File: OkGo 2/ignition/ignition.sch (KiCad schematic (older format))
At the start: 45 parts, among them K101 16A SPST, P102 JST_XH_4WAY, P103 BATT, P104 BATT, P105 PPOLE, P106 PPOLE, P107 CHARGE_CASE, P108 SMA, SW101 LATCHING PUSH, U101 SWD, U102 FUSE 15A, U103 CLIP, U104 BEZEL, U105 RFM95W, U106 STM32F071CBT6, U107 TSR 0.5-2433, Y101 8MHz

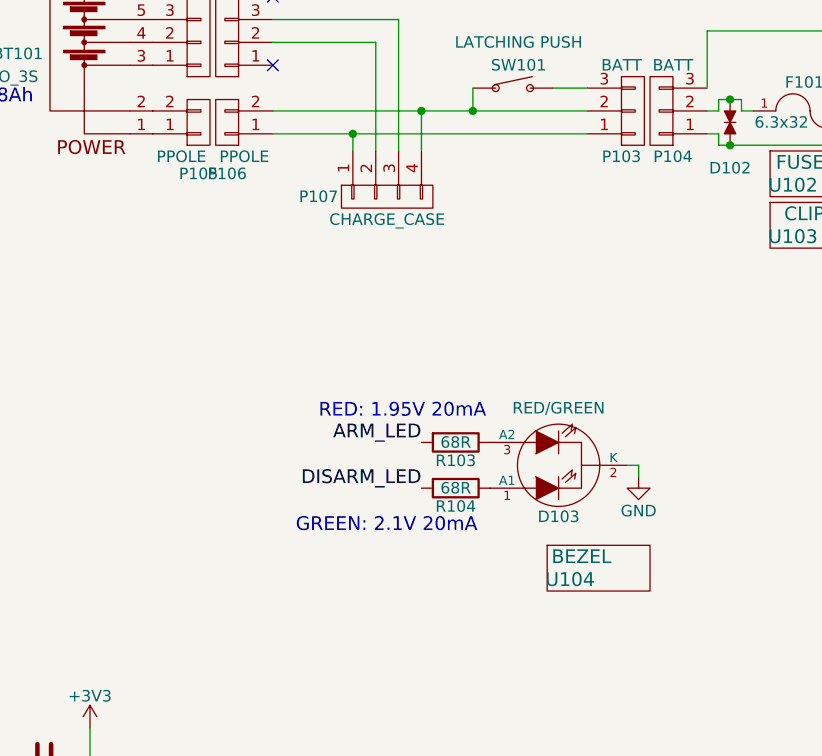
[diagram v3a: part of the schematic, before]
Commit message: 4-bit LCD, pulldowns, 2-pin bicolour ARM LED
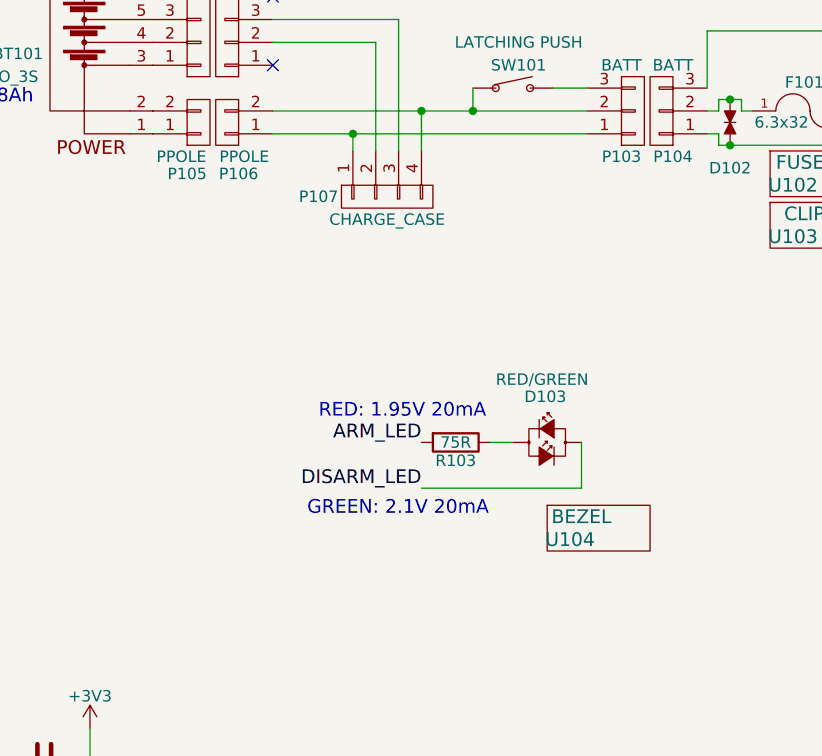
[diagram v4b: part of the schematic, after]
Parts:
- removed D103: RED/GREEN, symbol Led_x2
- removed R104: 68R, Resistors_SMD:R_0805, symbol R
- added D103: RED/GREEN, symbol LED_bicolour
- R103: value 68R -> 75R; Farnell 2332055 -> 2331781
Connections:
- net DISARM_LED: now also D103.2 (A)
- net at R103.1: now also D103.1 (K)
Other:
- moved on the sheet: U104
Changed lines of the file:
@@
 LIBS:push_illum
 LIBS:push_illum_straight
+LIBS:led_bicolour
 LIBS:ignition-cache
 EELAYER 25 0
@@
 $EndComp
 $Comp
-L Led_x2 D103
-U 1 1 55A8E3E4
-P 3500 2800
-F 0 "D103" H 3500 3025 50  0000 C CNN
-F 1 "RED/GREEN" H 3500 2550 50  0000 C CNN
-F 2 "" H 3500 2800 60  0000 C CNN
-F 3 "" H 3500 2800 60  0000 C CNN
-F 4 "2449761" H 3500 2800 60  0001 C CNN "Farnell"
-	1    3500 2800
-	-1   0    0    1
-$EndComp
-$Comp
-L GND #PWR021
-U 1 1 55A8E7EB
-P 3850 2850
-F 0 "#PWR021" H 3850 2600 50  0001 C CNN
-F 1 "GND" H 3850 2700 50  0000 C CNN
-F 2 "" H 3850 2850 60  0000 C CNN
-F 3 "" H 3850 2850 60  0000 C CNN
-	1    3850 2850
-	1    0    0    -1
-$EndComp
-$Comp
 L R R103
 U 1 1 55A8E9D5
 P 3050 2700
 F 0 "R103" V 3130 2700 50  0000 C CNN
-F 1 "68R" V 3050 2700 50  0000 C CNN
+F 1 "75R" V 3050 2700 50  0000 C CNN
 F 2 "Resistors_SMD:R_0805" V 2980 2700 30  0001 C CNN
 F 3 "" H 3050 2700 30  0000 C CNN
-F 4 "2332055" H 3050 2700 60  0001 C CNN "Farnell"
+F 4 "2331781" H 3050 2700 60  0001 C CNN "Farnell"
 	1    3050 2700
-	0    1    1    0
-$EndComp
-$Comp
-L R R104
-U 1 1 55A8EA84
-P 3050 2900
-F 0 "R104" V 3130 2900 50  0000 C CNN
-F 1 "68R" V 3050 2900 50  0000 C CNN
-F 2 "Resistors_SMD:R_0805" V 2980 2900 30  0001 C CNN
-F 3 "" H 3050 2900 30  0000 C CNN
-F 4 "2332055" H 3050 2900 60  0001 C CNN "Farnell"
-	1    3050 2900
 	0    1    1    0
 $EndComp
@@
 L PART U104
 U 1 1 55A94007
-P 3500 3300
-F 0 "U104" H 3550 3300 60  0000 C CNN
-F 1 "BEZEL" H 3600 3400 60  0000 C CNN
-F 2 "" H 3500 3300 60  0000 C CNN
-F 3 "" H 3500 3300 60  0000 C CNN
-F 4 "SC11628" H 3500 3300 60  0001 C CNN "Farnell"
-	1    3500 3300
+P 3500 3125
+F 0 "U104" H 3550 3125 60  0000 C CNN
+F 1 "BEZEL" H 3600 3225 60  0000 C CNN
+F 2 "" H 3500 3125 60  0000 C CNN
+F 3 "" H 3500 3125 60  0000 C CNN
+F 4 "SC11628" H 3500 3125 60  0001 C CNN "Farnell"
+	1    3500 3125
 	1    0    0    -1
 $EndComp
 Text Notes 2450 2600 0    60   ~ 0
 RED: 1.95V 20mA
-Text Notes 2350 3100 0    60   ~ 0
+Text Notes 2400 3025 0    60   ~ 0
 GREEN: 2.1V 20mA
 $Comp
@@
 Wire Wire Line
 	3475 1150 3625 1150
-Wire Wire Line
-	3850 2850 3850 2800
-Wire Wire Line
-	3850 2800 3800 2800
 Wire Wire Line
 	6650 6400 6650 6250
@@
 U 1 1 55AB8DCF
 P 2050 1300
-F 0 "P106" H 2050 1525 50  0000 C CNN
+F 0 "P106" H 2000 1525 50  0000 C CNN
 F 1 "PPOLE" H 1975 1450 50  0000 C CNN
 F 2 "" H 2050 1300 60  0000 C CNN
@@
 U 1 1 55ABB267
 P 1925 1300
-F 0 "P105" H 1925 1525 50  0000 C CNN
+F 0 "P105" H 1875 1525 50  0000 C CNN
 F 1 "PPOLE" H 1850 1450 50  0000 C CNN
 F 2 "" H 1925 1300 60  0000 C CNN
@@
 	2900 1250 2900 1425
 Connection ~ 2900 1250
+$Comp
+L LED_bicolour D103
+U 1 1 55BB39DE
+P 3450 2700
+F 0 "D103" H 3350 2900 50  0000 L CNN
+F 1 "RED/GREEN" H 3225 2975 50  0000 L CNN
+F 2 "" V 3450 2760 60  0000 C CNN
+F 3 "" V 3450 2760 60  0000 C CNN
+F 4 "1581207" H 3450 2700 60  0001 C CNN "Farnell"
+	1    3450 2700
+	1    0    0    -1
+$EndComp
+Wire Wire Line
+	2900 2900 3600 2900
+Wire Wire Line
+	3200 2700 3300 2700
+Wire Wire Line
+	3600 2900 3600 2700
 $EndSCHEMATC

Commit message: Finished demo-route of control
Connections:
- net GND: now also U106.44 (BOOT0)
- net nRST: now also U106.7 (NRST); no longer U106.44 (BOOT0)
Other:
- moved on the sheet: C104, TP103
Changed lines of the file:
@@
 L C C104
 U 1 1 5562F811
-P 4000 4600
-F 0 "C104" H 3900 4700 50  0000 L CNN
-F 1 "100n" H 3800 4500 50  0000 L CNN
-F 2 "Capacitors_SMD:C_0805" H 4038 4450 30  0001 C CNN
-F 3 "" H 4000 4600 60  0000 C CNN
-F 4 "2407344" H 4000 4600 60  0001 C CNN "Farnell"
-	1    4000 4600
+P 4000 4500
+F 0 "C104" H 3900 4600 50  0000 L CNN
+F 1 "100n" H 3800 4400 50  0000 L CNN
+F 2 "Capacitors_SMD:C_0805" H 4038 4350 30  0001 C CNN
+F 3 "" H 4000 4500 60  0000 C CNN
+F 4 "2407344" H 4000 4500 60  0001 C CNN "Farnell"
+	1    4000 4500
 	-1   0    0    -1
 $EndComp
@@
 L GND #PWR013
 U 1 1 5562F9AC
-P 3950 4800
-F 0 "#PWR013" H 3950 4550 50  0001 C CNN
-F 1 "GND" H 3950 4650 50  0000 C CNN
-F 2 "" H 3950 4800 60  0000 C CNN
-F 3 "" H 3950 4800 60  0000 C CNN
-	1    3950 4800
+P 3950 4700
+F 0 "#PWR013" H 3950 4450 50  0001 C CNN
+F 1 "GND" H 3950 4550 50  0000 C CNN
+F 2 "" H 3950 4700 60  0000 C CNN
+F 3 "" H 3950 4700 60  0000 C CNN
+	1    3950 4700
 	-1   0    0    -1
 $EndComp
@@
 Text Label 5900 5550 0    60   ~ 0
 RFM_RESET
-Text Label 4200 4450 0    60   ~ 0
+Text Label 4200 4350 0    60   ~ 0
 nRST
 $Comp
@@
 L TestPoint TP103
 U 1 1 559DC7C1
-P 3850 4450
-F 0 "TP103" H 3850 4375 60  0000 C CNN
-F 1 "nRST" H 3825 4275 60  0000 C CNN
-F 2 "common:TESTPOINT" H 3850 4450 60  0001 C CNN
-F 3 "" H 3850 4450 60  0000 C CNN
-	1    3850 4450
+P 3850 4350
+F 0 "TP103" H 3850 4275 60  0000 C CNN
+F 1 "nRST" H 3825 4175 60  0000 C CNN
+F 2 "common:TESTPOINT" H 3850 4350 60  0001 C CNN
+F 3 "" H 3850 4350 60  0000 C CNN
+	1    3850 4350
 	-1   0    0    1
 $EndComp
@@
 Connection ~ 1800 5450
 Wire Wire Line
-	3850 4750 4000 4750
-Wire Wire Line
-	3950 4750 3950 4800
-Connection ~ 3950 4750
-Wire Wire Line
-	3750 4450 4200 4450
-Wire Wire Line
-	3750 4450 3750 4700
-Wire Wire Line
-	3750 4700 3300 4700
-Wire Wire Line
-	3850 4750 3850 4800
-Wire Wire Line
-	3850 4800 3300 4800
+	3850 4650 4000 4650
+Wire Wire Line
+	3950 4650 3950 4700
+Connection ~ 3950 4650
+Wire Wire Line
+	3750 4350 4200 4350
+Wire Wire Line
+	3750 4350 3750 4600
+Wire Wire Line
+	3750 4600 3300 4600
+Wire Wire Line
+	3850 4650 3850 4700
+Wire Wire Line
+	3850 4700 3300 4700
 Wire Wire Line
 	3300 5300 4100 5300
@@
 Wire Wire Line
 	8800 6050 8750 6050
-Connection ~ 4000 4450
+Connection ~ 4000 4350
 Connection ~ 6350 1150
 Connection ~ 6350 1250
 Connection ~ 6550 6400
-Connection ~ 3850 4450
+Connection ~ 3850 4350
 Wire Wire Line
 	3300 5400 3750 5400

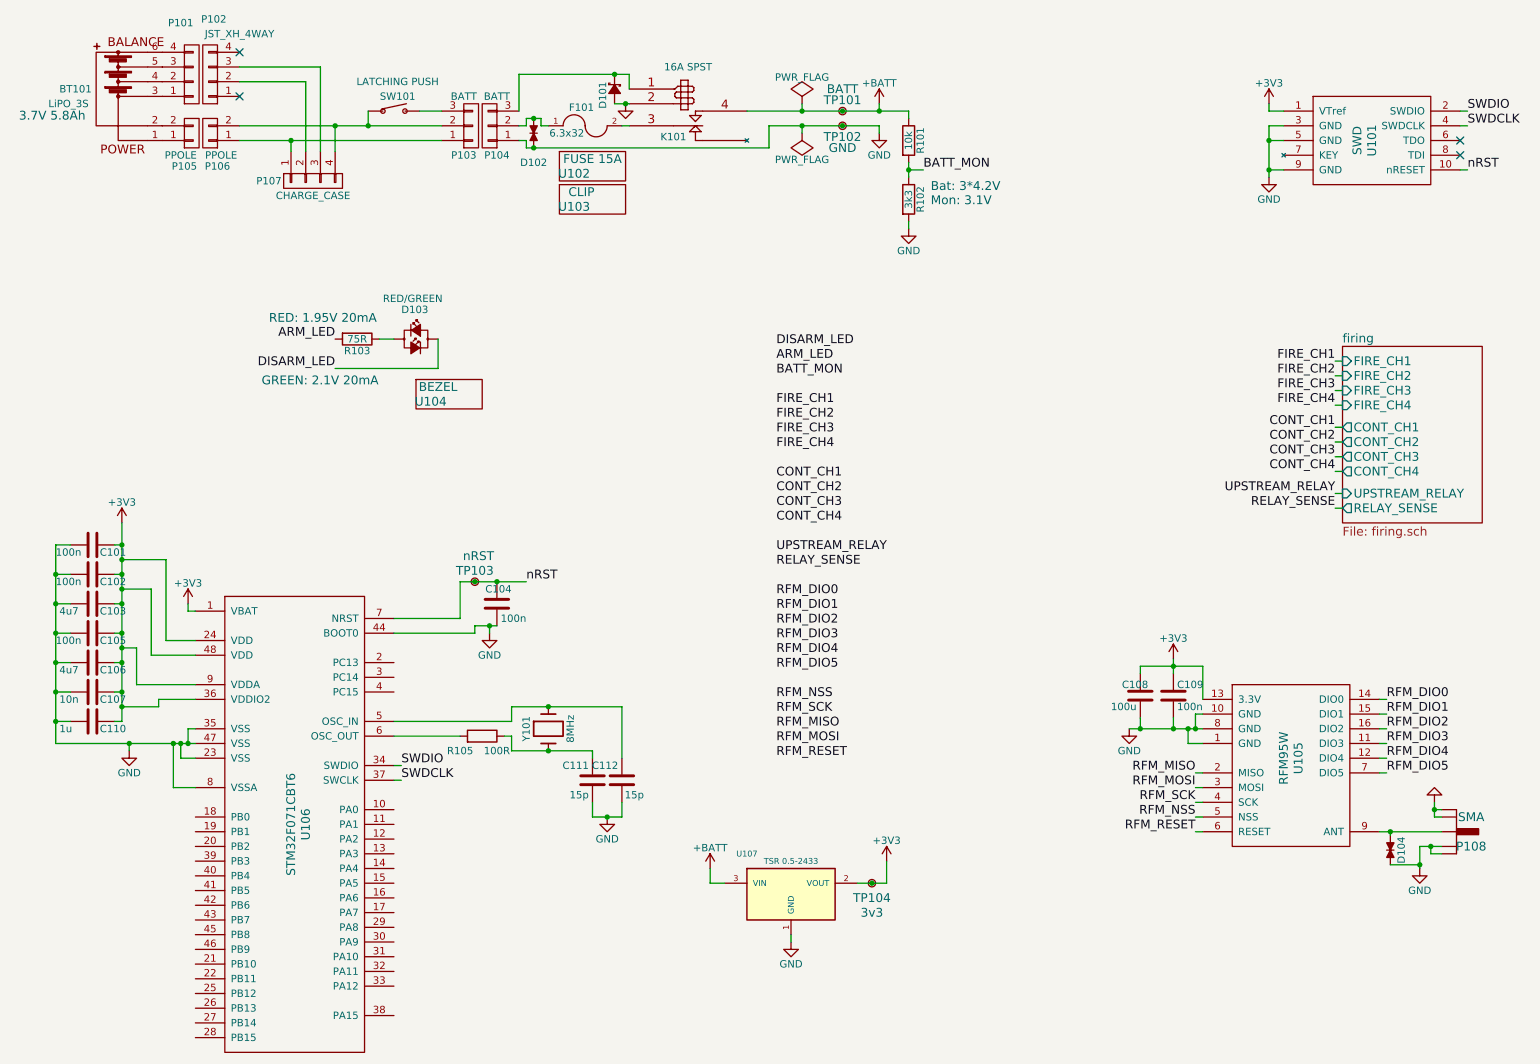
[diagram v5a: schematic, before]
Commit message: Footprinting, rockers
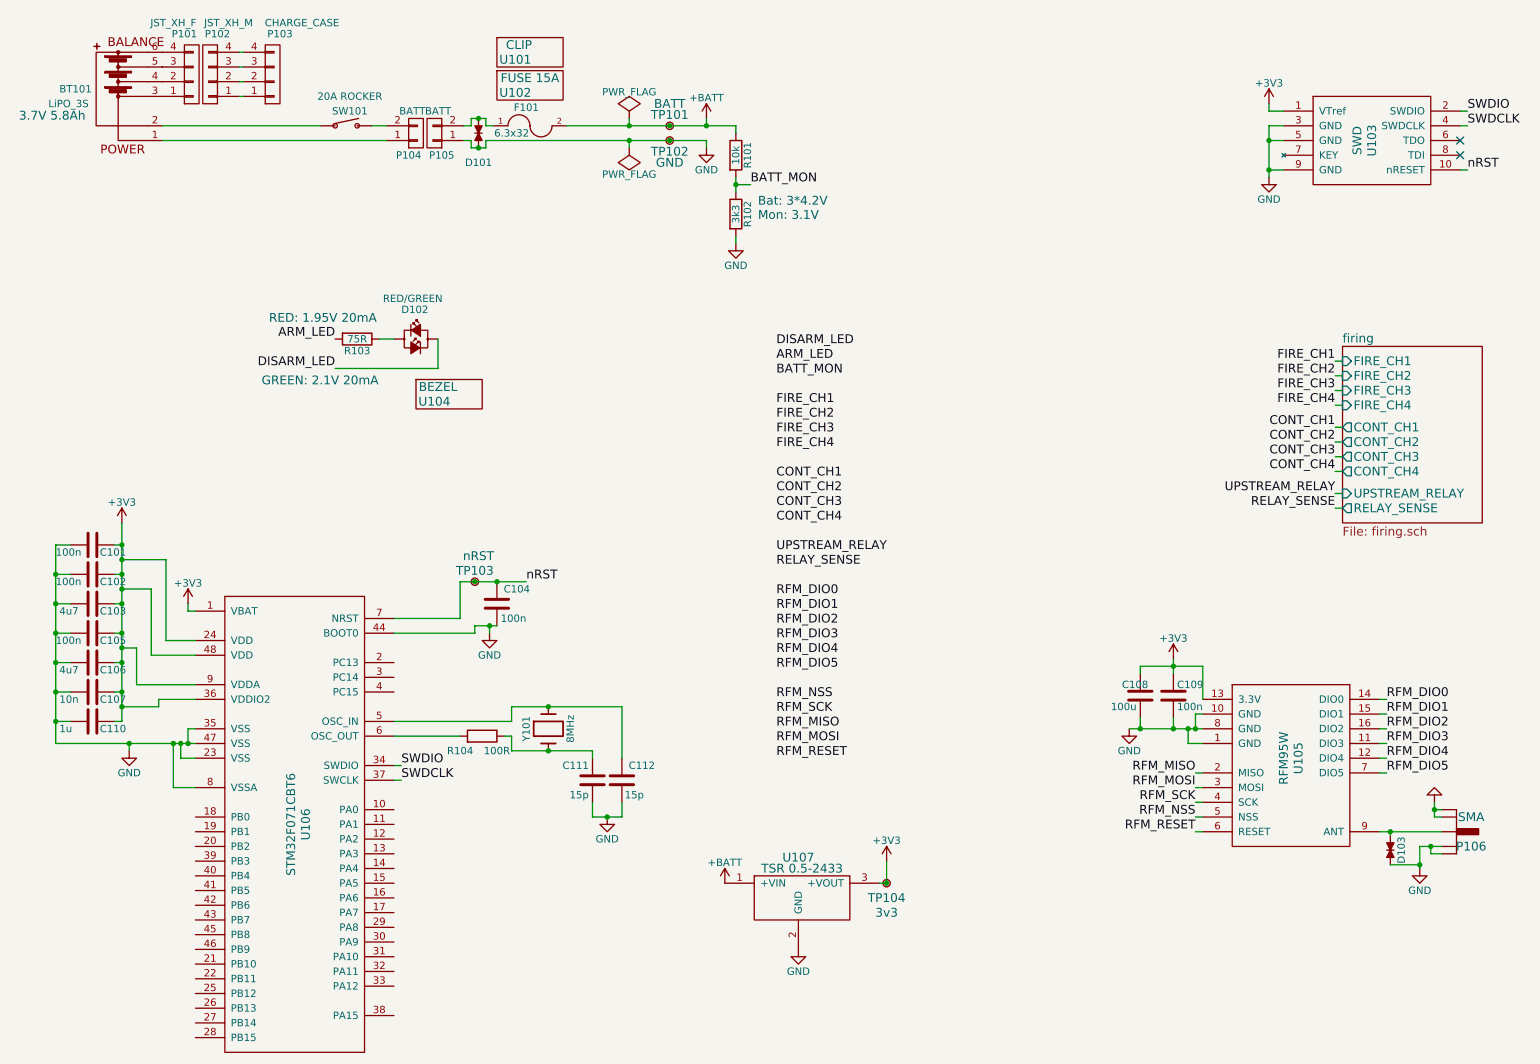
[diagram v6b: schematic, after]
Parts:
- removed D101: MBR2H200SFT1G, ignition:SOD-123FL, symbol D_Schottky_Small
- removed K101: 16A SPST, ignition:Relay_RT314, symbol RELAY_SPST
- removed P103, P104: BATT, symbol CONN_01X03
- removed P106: PPOLE, symbol CONN_01X02
- removed U107: TSR 0.5-2433, SOT-23, symbol APE8865N-33-HF-3
- added P104: BATT, symbol CONN_01X02
- added U107: TSR 0.5-2433, ignition:TSR-0_5, symbol TSR-0_5
- P101: value ~ -> JST_XH_F
- P102: value JST_XH_4WAY -> JST_XH_M
- P105: value PPOLE -> BATT; footprint (none) -> ignition:PCB_SPADE; Farnell (none) -> 2308798
- SW101: value LATCHING PUSH -> 20A ROCKER; Farnell SW02719 -> 1839503
- renumbered D102 to D101, D103 to D102, D104 to D103, P107 to P103, P108 to P106, R105 to R104, U103 to U101, U101 to U103
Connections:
- net +3V3: now also U107.3 (+VOUT)
- net +BATT: now also F101.2, U107.1 (+VIN)
- net GND: now also P105.1 (P1), U107.2 (GND)
- net at D101.1, F101.1: now also P105.2 (P2)
- net at BT101.1: now also P104.1 (P1); no longer P105.1 (P1)
- net at BT101.2: now also SW101.1; no longer P105.2 (P2)
- net at P103.1 (P1): now also P102.1 (P1)
- net at P103.4 (P4): now also P102.4 (P4); no longer SW101.1
- net at SW101.2: now also P104.2 (P2)
- no-connect marks 4 -> 2
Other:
- moved on the sheet: D101, F101, P103, R101, R102, SW101, TP101, TP102, TP104, U101, U102
